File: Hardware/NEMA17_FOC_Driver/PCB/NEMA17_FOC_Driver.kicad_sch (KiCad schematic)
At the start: 33 parts, among them J1 Conn_01x02_Pin, J2 Conn_01x02_Pin, U1 DRV8844PWPR, U2 AP63203WU-7, U3 MT6701CT, U4 STM32G431KBTx, U5 TCAN332

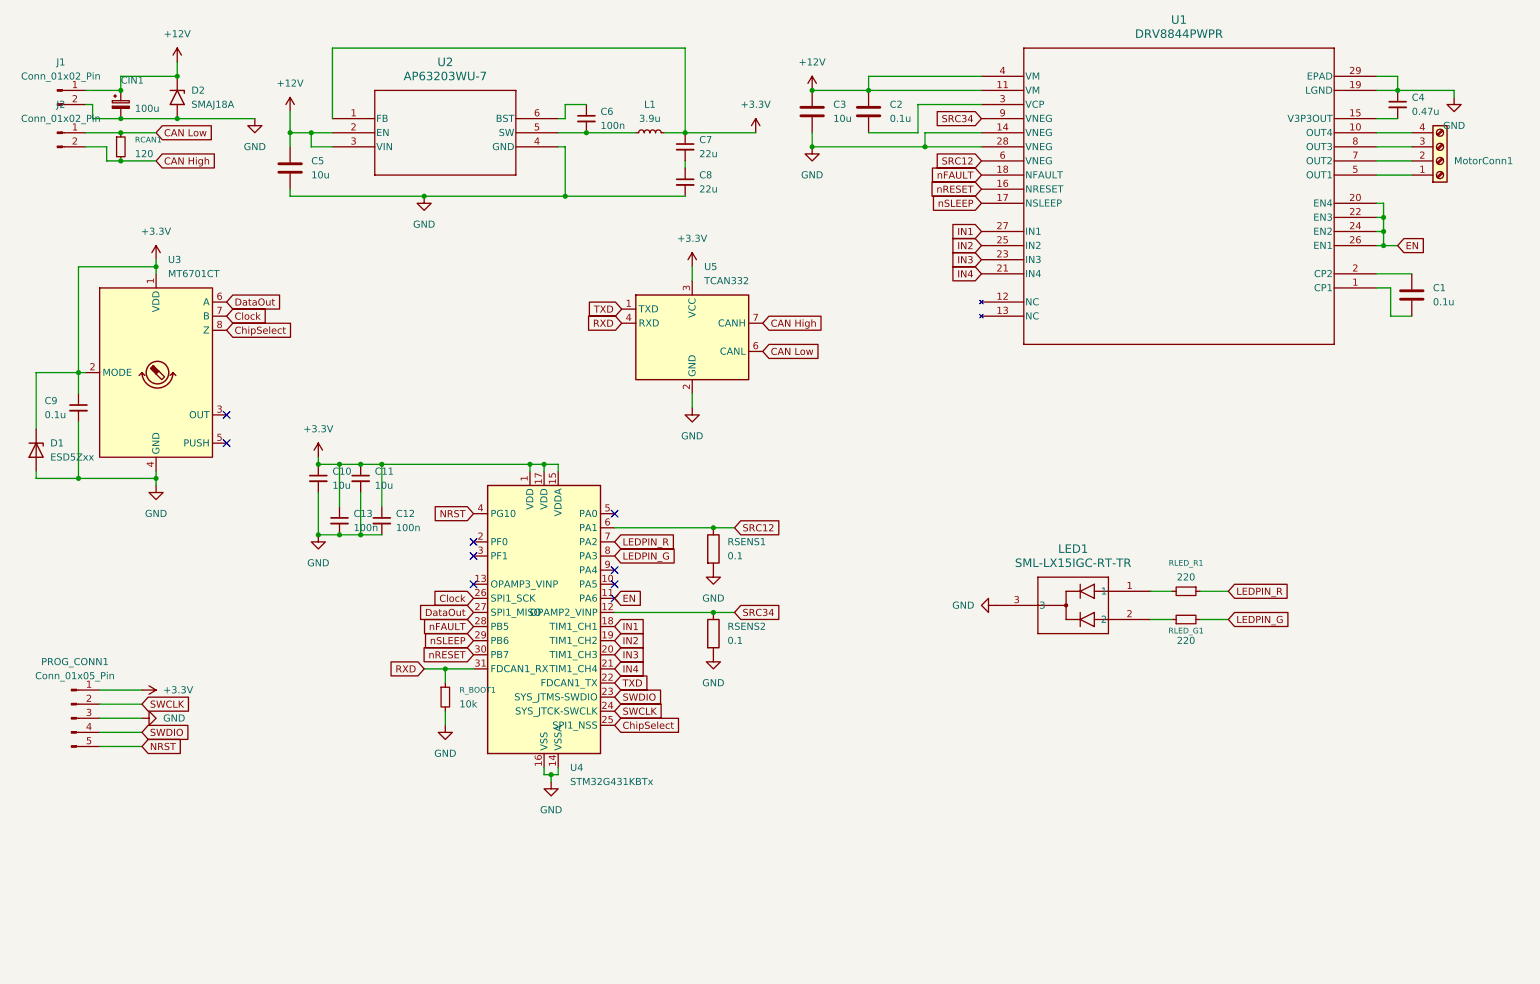
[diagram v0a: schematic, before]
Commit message: Firmware structure, schematic for PCB V2.0, layout still pending.
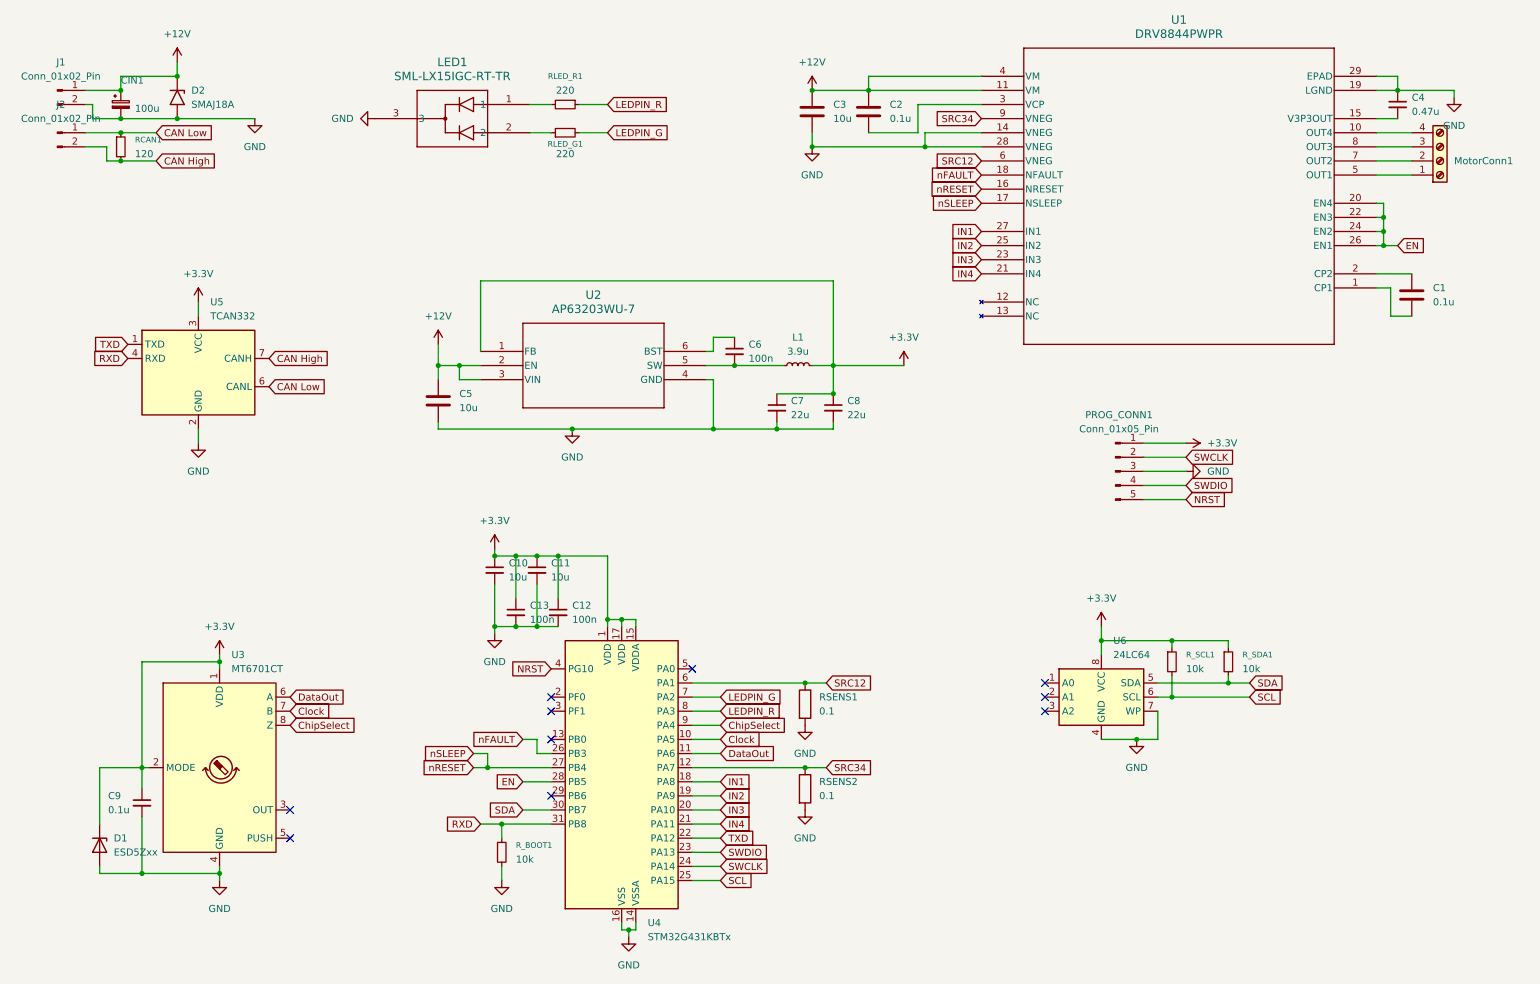
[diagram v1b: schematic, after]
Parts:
- added R_SCL1, R_SDA1: 10k, Resistor_SMD:R_0603_1608Metric, symbol Device:R_Small
- added U6: 24LC64, Package_SO:TSSOP-8_3x3mm_P0.65mm, symbol Memory_EEPROM:24LC64
- LED1: footprint SML:SML-LX15_LUM -> SML-LX15:SML-LX15_LUM
- PROG_CONN1: footprint TestPoint:TestPoint_Pad_D1.0mm -> Connector_JST:JST_EH_B5B-EH-A_1x05_P2.50mm_Vertical
- U1: footprint DRV8844:PWP28_5P18X3P1-L -> DRV8844:PWP28_5P18X3P1-M
- U2: footprint AP63203:AP63203WU-7_DIO-L -> AP63203WU:AP63203WU-7_DIO-L
- U5: footprint TCAN332:D0008A_L -> TCAN332:D0008A_M
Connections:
- net +3.3V: now also C8.1, R_SCL1.1, R_SDA1.1, U6.8 (VCC)
- net ChipSelect: now also U4.9 (PA4); no longer U4.25 (PA15)
- net Clock: now also U4.10 (PA5); no longer U4.26 (PB3)
- net DataOut: now also U4.11 (PA6); no longer U4.27 (PB4)
- net EN: now also U4.28 (PB5); no longer U4.11 (PA6)
- net GND: now also C7.2, U6.4 (GND), U6.7 (WP)
- net LEDPIN_G: now also U4.7 (PA2); no longer U4.8 (PA3)
- net LEDPIN_R: now also U4.8 (PA3); no longer U4.7 (PA2)
- net nFAULT: now also U4.26 (PB3); no longer U4.28 (PB5)
- net nRESET: now also U1.17 (NSLEEP), U4.27 (PB4); no longer U4.30 (PB7)
- net nSLEEP: no longer names the net of U4.29 (PB6)
- net nSLEEP: no longer U1.17 (NSLEEP)
- new net SCL: R_SCL1.2, U4.25 (PA15), U6.6 (SCL)
- new net SDA: R_SDA1.2, U4.30 (PB7), U6.5 (SDA)
- no-connect marks 9 -> 10
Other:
- moved on the sheet: C10, C11, C12, C13, C5, C6, C7, C8, C9, D1, L1, LED1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
